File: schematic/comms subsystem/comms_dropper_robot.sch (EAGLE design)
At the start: 22 parts, among them IC1 TP4056, IC2 FS8205A, Q1 IRF4905

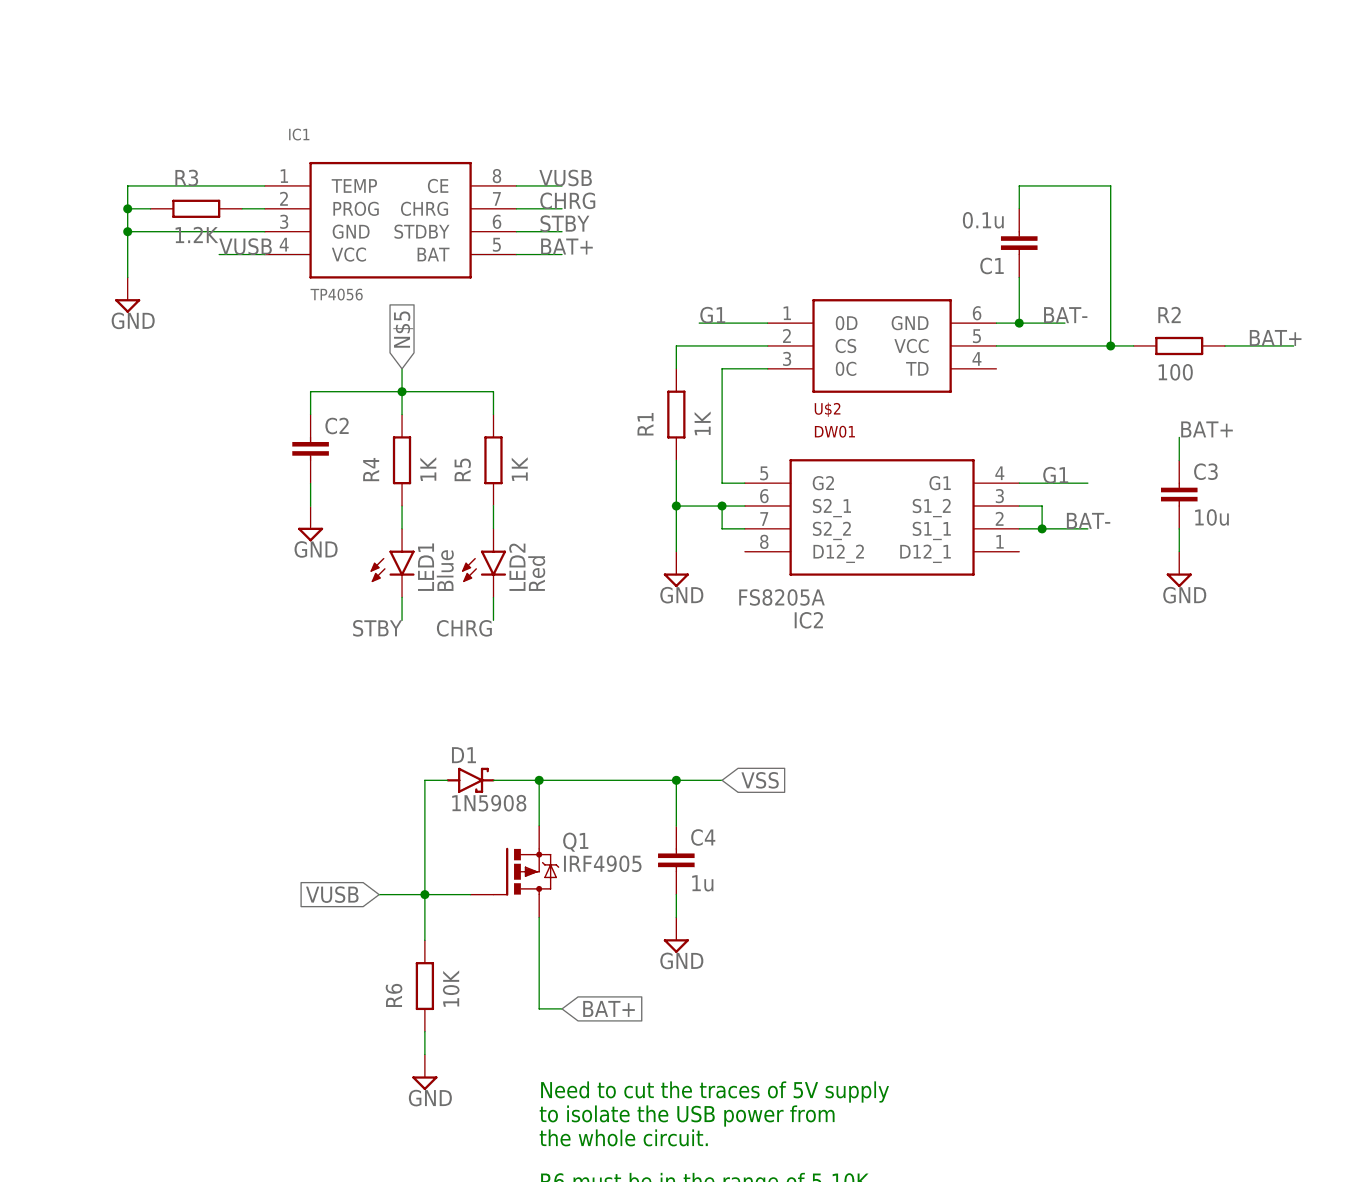
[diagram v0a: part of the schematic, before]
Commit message: added by Sean, modified for comms subsystem design
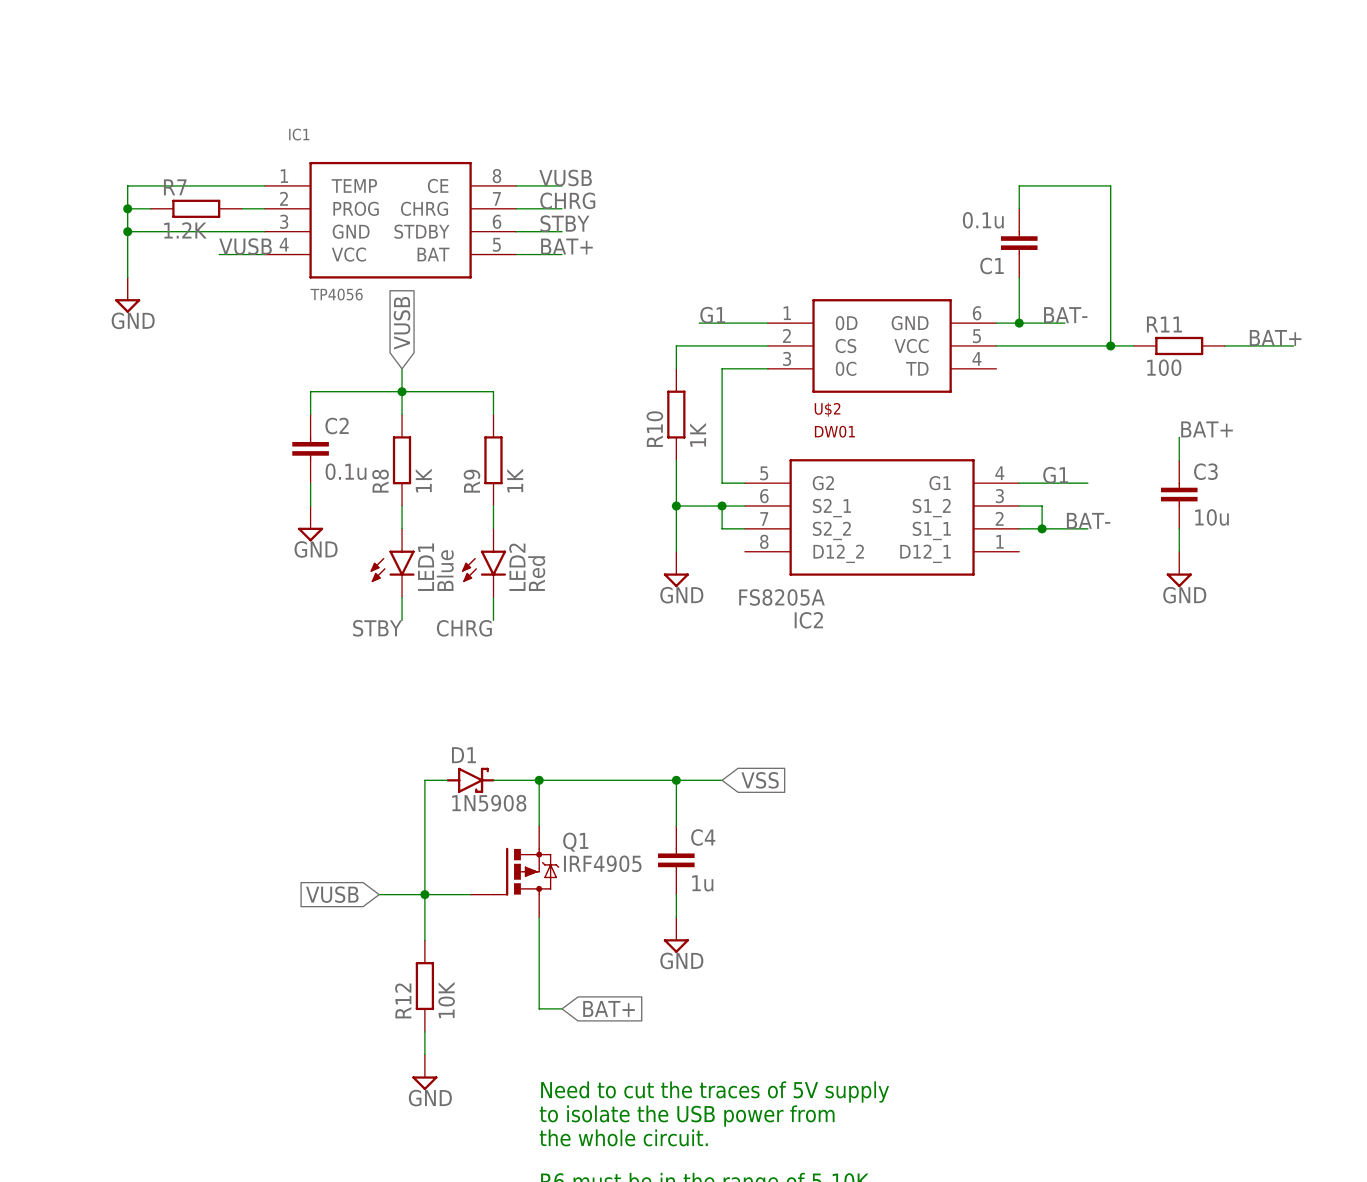
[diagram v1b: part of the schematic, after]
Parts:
- removed R1, R4, R5: 1K, ngspice-simulation:R
- removed R2: 100, ngspice-simulation:R
- removed R3: 1.2K, ngspice-simulation:R
- removed R6: 10K, ngspice-simulation:R
- added R10, R8, R9: 1K, rcl:R-EU_R0805
- added R11: 100, rcl:R-EU_R0805
- added R12: 10K, rcl:R-EU_R0805
- added R7: 1.2K, rcl:R-EU_R0805
- C2: value (none) -> 0.1u
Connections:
- removed net N$5: C2.1, R4.2, R5.2
- net BAT+: now also R11.2; no longer R2.2
- net GND: now also R10.1, R12.1, R7.1; no longer R1.1, R3.1, R6.1
- net N$2: now also R7.2; no longer R3.2
- net N$3: now also R10.2; no longer R1.2
- net N$4: now also R11.1; no longer R2.1
- net N$7: now also R8.1; no longer R4.1
- net N$8: now also R9.1; no longer R5.1
- net VUSB: now also C2.1, R12.2, R8.2, R9.2; no longer R6.2
